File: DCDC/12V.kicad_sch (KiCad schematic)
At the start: 25 parts, among them M1-3 30V 60A, M2-3 30V 35A

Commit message: pcb designed for 3 outputs
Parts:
- IC-3: footprint Library:RGY0020B -> RGY0020B
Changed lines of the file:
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@@
       (effects (font (size 1.27 1.27)) (justify left))
     )
-    (property "Footprint" "Library:RGY0020B" (at 149.86 158.42 0)
+    (property "Footprint" "RGY0020B" (at 149.86 158.42 0)
       (effects (font (size 1.27 1.27)) (justify left top) hide)
     )
@@
       (effects (font (size 1.27 1.27)) hide)
     )
-    (property "Datasheet" "https://hu.mouser.com/datasheet/2/420/PSGLL_e-2507380.pdf" (at 228.6 102.87 0)
+    (property "Datasheet" "~" (at 228.6 102.87 0)
       (effects (font (size 1.27 1.27)) hide)
     )
@@
       (effects (font (size 1.27 1.27)) hide)
     )
-    (property "Datasheet" "https://www.allaboutcircuits.com/tools/coil-inductance-calculator/" (at 190.5 76.2 0)
+    (property "Datasheet" "~" (at 190.5 76.2 0)
       (effects (font (size 1.27 1.27)) hide)
     )
@@
       (effects (font (size 1.27 1.27)) hide)
     )
-    (property "Datasheet" "https://hu.mouser.com/datasheet/2/240/media-3320211.pdf" (at 179.07 72.39 0)
-      (effects (font (size 1.27 1.27)) hide)
-    )
+    (property "Datasheet" "https://ngspice.sourceforge.io/docs/ngspice-manual.pdf" (at 179.07 72.39 0)
+      (effects (font (size 1.27 1.27)) hide)
+    )

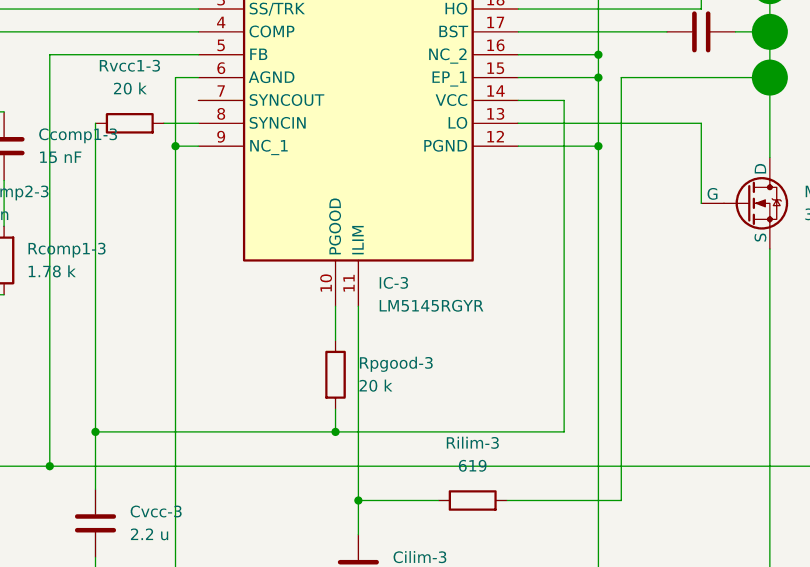
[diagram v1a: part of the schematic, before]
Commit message: dcdc simulation, mechanical drawings
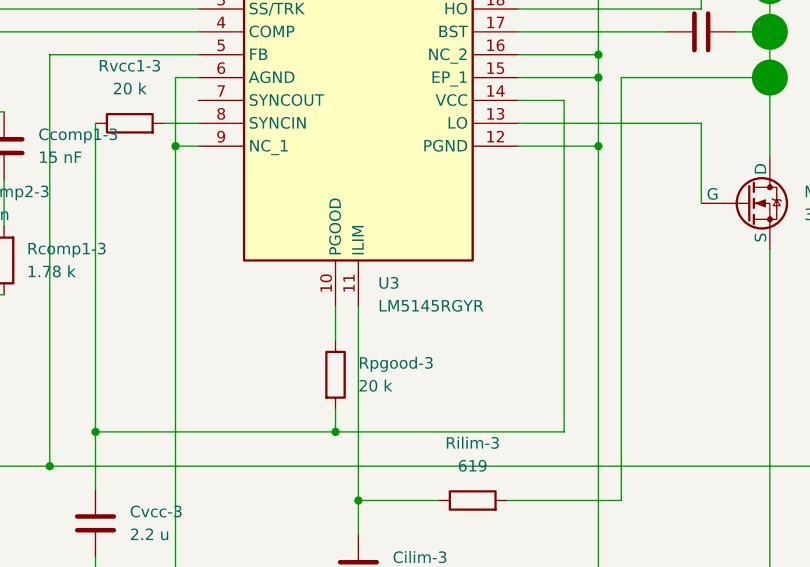
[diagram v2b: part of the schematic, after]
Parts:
- renumbered IC-3 to U3

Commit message: one module of the dcdc converter seems ready again...
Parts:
- removed M1-3: 30V 60A, Library:TO545P521X1594X2566-3P, symbol Simulation_SPICE:NMOS
- removed M2-3: 30V 35A, Library:TO545P521X1594X2566-3P, symbol Simulation_SPICE:NMOS
- added M1-3: 30V 60A, Library:TO545P521X1594X2566-3P, symbol Local:IXFX360N10T
- added M2-3: 30V 35A, Library:TO545P521X1594X2566-3P, symbol Local:IXFX360N10T
- U3: footprint RGY0020B -> Library:RGY0020B
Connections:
- net GND: now also M2-3.3
- net Vin: now also Cin-3.1, Ruv1-3.1, Rvin-3.1, M1-3.2
- net at U3.13 (LO): now also M2-3.1
- net at U3.18 (HO): now also M1-3.1
- net at Cbst-3.2, L1-3.1, Rilim-3.2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: now also M1-3.3, M2-3.2

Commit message: 3 modules of DCDC, hinge
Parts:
- L1-3: Manufacturer_Part_Number R=15,L=2.145,N=11,d=1.95, Rwire=1.68 mOhm -> D=15mm,N=20,L=20mm,d=2mm
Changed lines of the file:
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@@
 			)
 		)
-		(property "Datasheet" "~"
+		(property "Datasheet" "https://www.allaboutcircuits.com/tools/coil-inductance-calculator/"
 			(at 190.5 76.2 0)
 			(effects
@@
 			)
 		)
-		(property "Manufacturer_Part_Number" "R=15,L=2.145,N=11,d=1.95, Rwire=1.68 mOhm"
+		(property "Manufacturer_Part_Number" "D=15mm,N=20,L=20mm,d=2mm"
 			(at 190.5 76.2 0)
 			(effects

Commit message: DCDC fix unavailable parts, BMS redesign, handle fix, rearrange top half
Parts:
- Cbst-3: Manufacturer_Part_Number GRM188R61E104KA01D -> C0603C104J1RACAUTO
- Ruv1-3: footprint Resistor_SMD:R_0201_0603Metric -> Resistor_SMD:R_0603_1608Metric; Manufacturer_Part_Number RC0201FR-7D68K1L -> ERA-3VEB6812V
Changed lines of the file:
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@@
 			)
 		)
-		(property "Footprint" "Resistor_SMD:R_0201_0603Metric"
+		(property "Footprint" "Resistor_SMD:R_0603_1608Metric"
 			(at 64.262 41.91 90)
 			(effects
@@
 			)
 		)
-		(property "Manufacturer_Part_Number" "RC0201FR-7D68K1L"
+		(property "Manufacturer_Part_Number" "ERA-3VEB6812V"
 			(at 66.04 41.91 0)
 			(effects
@@
 			)
 		)
-		(property "Manufacturer_Part_Number" "GRM188R61E104KA01D"
+		(property "Manufacturer_Part_Number" "C0603C104J1RACAUTO"
 			(at 173.99 81.28 0)
 			(effects

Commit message: coil redesign, materials
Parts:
- L1-3: Manufacturer_Part_Number D=15mm,N=20,L=20mm,d=2mm -> D=21mm,N=12,L=13.5mm,d=1.12mm
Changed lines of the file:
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@@
 			)
 		)
-		(property "Manufacturer_Part_Number" "D=15mm,N=20,L=20mm,d=2mm"
+		(property "Manufacturer_Part_Number" "D=21mm,N=12,L=13.5mm,d=1.12mm"
 			(at 190.5 76.2 0)
 			(effects
